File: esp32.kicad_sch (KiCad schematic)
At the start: 22 parts, among them J3 serial, Q2 Q_NPN_BCE, Q3 Q_NPN_BCE, U26 ESP32-WROOM-32D, U28 LMZM23601

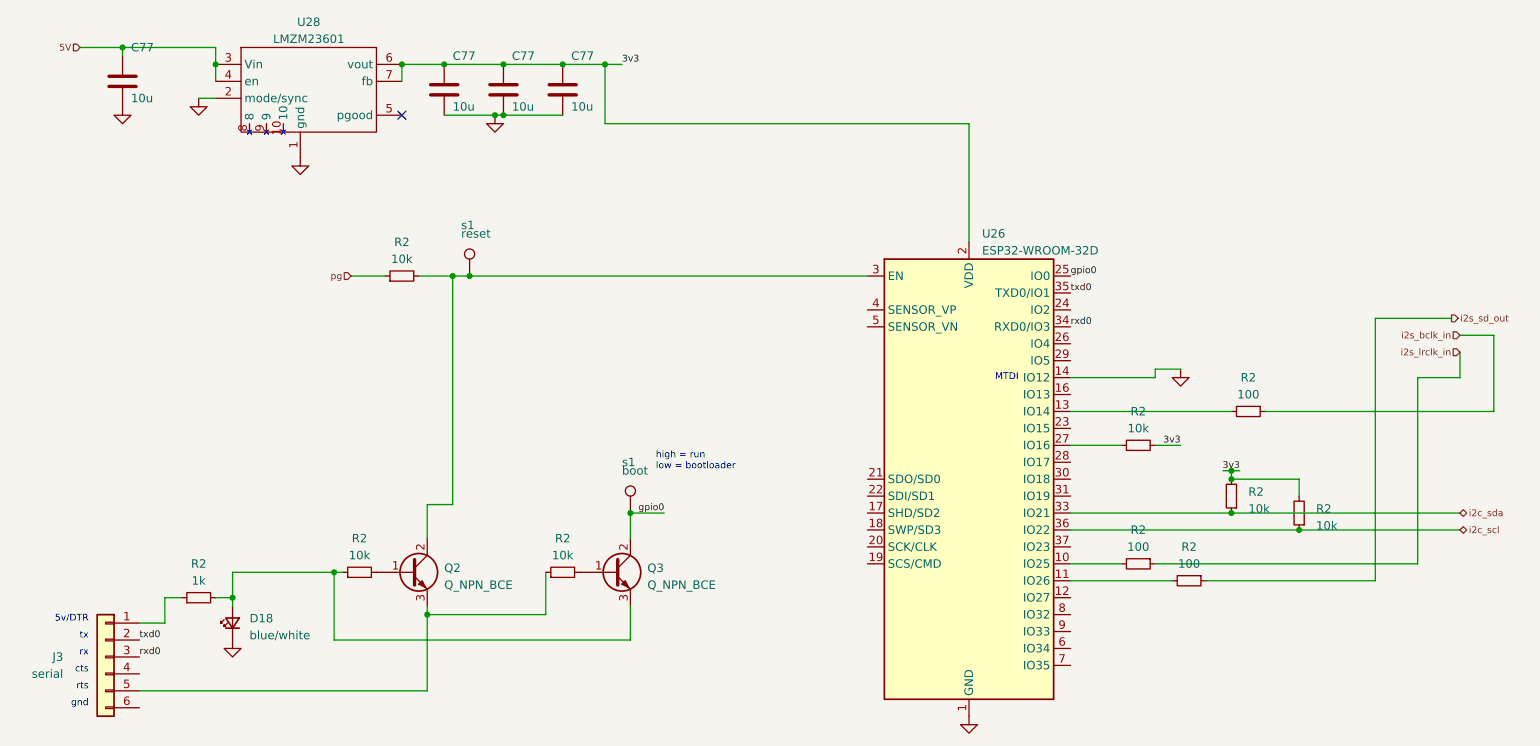
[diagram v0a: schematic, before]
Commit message: update to kicad 8
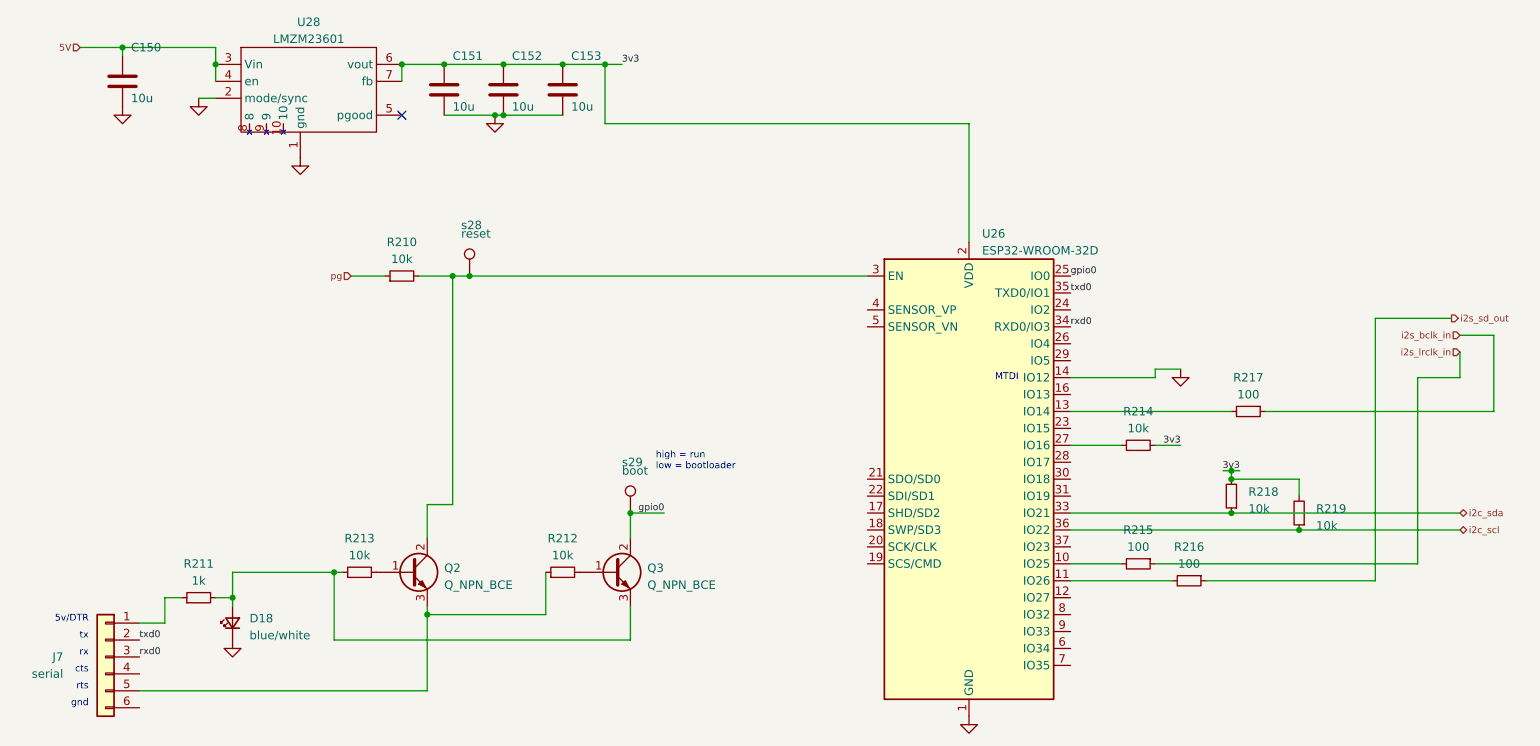
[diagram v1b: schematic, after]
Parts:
- renumbered C77 to C150, C77 to C151, C77 to C152, C77 to C153, J3 to J7, R2 to R210, R2 to R211, R2 to R212, R2 to R213, R2 to R214, R2 to R215, R2 to R216, R2 to R217, R2 to R218, R2 to R219, s1 to s28, s1 to s29

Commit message: schematic: some fixes
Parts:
- added R222: 10k, invendelirium_audio:R_0603, symbol Device:R_Small
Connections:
- net GND: now also R222.2; no longer U26.14 (IO12)
- new net: R222.1, U26.14 (IO12)
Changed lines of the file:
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@@
 	(wire
 		(pts
-			(xy 189.23 73.66) (xy 193.04 73.66)
+			(xy 191.77 73.66) (xy 195.58 73.66)
 		)
 		(stroke
@@
 	(wire
 		(pts
-			(xy 189.23 74.93) (xy 189.23 73.66)
+			(xy 191.77 74.93) (xy 191.77 73.66)
 		)
 		(stroke
@@
 	(wire
 		(pts
+			(xy 187.96 74.93) (xy 191.77 74.93)
+		)
+		(stroke
+			(width 0)
+			(type default)
+		)
+	)
+	(wire
+		(pts
 			(xy 222.25 105.41) (xy 196.85 105.41)
 		)
@@
 	(wire
 		(pts
-			(xy 176.53 74.93) (xy 189.23 74.93)
+			(xy 176.53 74.93) (xy 182.88 74.93)
 		)
 		(stroke
@@
 	(symbol
 		(lib_id "power:GND")
-		(at 193.04 73.66 0)
+		(at 195.58 73.66 0)
 		(unit 1)
 		(exclude_from_sim no)
@@
 		(fields_autoplaced yes)
 		(property "Reference" "#PWR0184"
-			(at 193.04 80.01 0)
+			(at 195.58 80.01 0)
 			(effects
 				(font
@@
 		)
 		(property "Value" "GND"
-			(at 193.04 78.74 0)
+			(at 195.58 78.74 0)
 			(effects
 				(font
@@
 		)
 		(property "Footprint" ""
-			(at 193.04 73.66 0)
+			(at 195.58 73.66 0)
 			(effects
 				(font
@@
 		)
 		(property "Datasheet" ""
-			(at 193.04 73.66 0)
+			(at 195.58 73.66 0)
 			(effects
 				(font
@@
 		)
 		(property "Description" ""
-			(at 193.04 73.66 0)
+			(at 195.58 73.66 0)
 			(effects
 				(font
@@
 					(unit 1)
 				)
+			)
+		)
+	)
+	(symbol
+		(lib_id "Device:R_Small")
+		(at 185.42 74.93 90)
+		(unit 1)
+		(exclude_from_sim no)
+		(in_bom yes)
+		(on_board yes)
+		(dnp no)
+		(fields_autoplaced yes)
+		(property "Reference" "R222"
+			(at 185.42 69.85 90)
+			(effects
+				(font
+					(size 1.27 1.27)
+				)
+			)
+		)
+		(property "Value" "10k"
+			(at 185.42 72.39 90)
+			(effects
+				(font
+					(size 1.27 1.27)
+				)
+			)
+		)
+		(property "Footprint" "invendelirium_audio:R_0603"
+			(at 185.42 74.93 0)
+			(effects
+				(font
+					(size 1.27 1.27)
+				)
+				(hide yes)
+			)
+		)
+		(property "Datasheet" "~"
+			(at 185.42 74.93 0)
+			(effects
+				(font
+					(size 1.27 1.27)
+				)
+				(hide yes)
+			)
+		)
+		(property "Description" ""
+			(at 185.42 74.93 0)
+			(effects
+				(font
+					(size 1.27 1.27)
+				)
+				(hide yes)
+			)
+		)
+		(pin "1"
+		)
+		(pin "2"
+		)
+		(instances
+			(project "uberamp1"
+				(path "/310059c1-d84b-43e2-9c9a-0e426c534a12/c7f5e7f4-a933-42eb-8650-67011ef6e24d"
+					(reference "R222")
+					(unit 1)
+				)

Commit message: updates
* add line out
* fix almost all erc
* some more random edits
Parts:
- U26: PN (none) -> ESP32-WROOM-32E-N16
- U28: PN (none) -> LMZM23601
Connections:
- net GND: now also J7.6 (Pin_6)
- no-connect marks 1 -> 24
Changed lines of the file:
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@@
+	)
+	(no_connect
+		(at 176.53 118.11)
+	)
+	(no_connect
+		(at 146.05 95.25)
+	)
+	(no_connect
+		(at 176.53 90.17)
+	)
+	(no_connect
+		(at 176.53 113.03)
+	)
+	(no_connect
+		(at 146.05 97.79)
+	)
+	(no_connect
+		(at 176.53 87.63)
+	)
+	(no_connect
+		(at 146.05 67.31)
+	)
+	(no_connect
+		(at 146.05 92.71)
+	)
+	(no_connect
+		(at 146.05 64.77)
+	)
+	(no_connect
+		(at 36.83 119.38)
+	)
+	(no_connect
+		(at 176.53 110.49)
+	)
+	(no_connect
+		(at 176.53 115.57)
+	)
+	(no_connect
+		(at 176.53 92.71)
+	)
+	(no_connect
+		(at 176.53 107.95)
 	)
 	(no_connect
 		(at 76.2 35.56)
+	)
+	(no_connect
+		(at 146.05 90.17)
+	)
+	(no_connect
+		(at 146.05 100.33)
+	)
+	(no_connect
+		(at 176.53 77.47)
+	)
+	(no_connect
+		(at 176.53 64.77)
+	)
+	(no_connect
+		(at 146.05 102.87)
+	)
+	(no_connect
+		(at 176.53 72.39)
+	)
+	(no_connect
+		(at 176.53 100.33)
+	)
+	(no_connect
+		(at 176.53 69.85)
+	)
+	(no_connect
+		(at 176.53 82.55)
 	)
 	(wire
@@
 	)
 	(symbol
+		(lib_id "power:GND")
+		(at 36.83 124.46 0)
+		(unit 1)
+		(exclude_from_sim no)
+		(in_bom yes)
+		(on_board yes)
+		(dnp no)
+		(fields_autoplaced yes)
+		(property "Reference" "#PWR0195"
+			(at 36.83 130.81 0)
+			(effects
+				(font
+					(size 1.27 1.27)
+				)
+				(hide yes)
+			)
+		)
+		(property "Value" "GND"
+			(at 36.83 129.54 0)
+			(effects
+				(font
+					(size 1.27 1.27)
+				)
+				(hide yes)
+			)
+		)
+		(property "Footprint" ""
+			(at 36.83 124.46 0)
+			(effects
+				(font
+					(size 1.27 1.27)
+				)
+				(hide yes)
+			)
+		)
+		(property "Datasheet" ""
+			(at 36.83 124.46 0)
+			(effects
+				(font
+					(size 1.27 1.27)
+				)
+				(hide yes)
+			)
+		)
+		(property "Description" ""
+			(at 36.83 124.46 0)
+			(effects
+				(font
+					(size 1.27 1.27)
+				)
+				(hide yes)
+			)
+		)
+		(pin "1"
+		)
+		(instances
+			(project "uberamp1"
+				(path "/310059c1-d84b-43e2-9c9a-0e426c534a12/c7f5e7f4-a933-42eb-8650-67011ef6e24d"
+					(reference "#PWR0195")
+					(unit 1)
+				)
+			)
+		)
+	)
+	(symbol
 		(lib_id "invendelirium_ic:LMZM23601")
 		(at 63.5 33.02 0)
@@
 		)
 		(property "Description" ""
+			(at 63.5 33.02 0)
+			(effects
+				(font
+					(size 1.27 1.27)
+				)
+				(hide yes)
+			)
+		)
+		(property "PN" "LMZM23601"
 			(at 63.5 33.02 0)
 			(effects
@@
 			(at 161.29 90.17 0)
 			(effects
+				(font
+					(size 1.27 1.27)
+				)
+				(hide yes)
+			)
+		)
+		(property "PN" "ESP32-WROOM-32E-N16"
+			(at 161.29 90.17 0)
+			(effects

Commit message: add power input +...
+ tons of fixes, footprint assignments, etc
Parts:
- renumbered C151 to CU28_1, C152 to CU28_2, C153 to CU28_3

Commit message: routing...
+ swap around dac channels, otherwise routing was crazy
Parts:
- U26: footprint RF_Module:ESP32-WROOM-32D -> invendelirium_audio:ESP32-WROOM-32D
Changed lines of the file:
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@@
 			)
 		)
-		(property "Footprint" "RF_Module:ESP32-WROOM-32D"
+		(property "Footprint" "invendelirium_audio:ESP32-WROOM-32D"
 			(at 177.8 124.46 0)
 			(effects

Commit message: lots of drc-related work
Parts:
- Q2, Q3: footprint PCM_4ms_Package_SOT:SOT23-3_PO123 -> invendelirium_general:SOT23-3_PO123
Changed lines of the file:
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@@
 			)
 		)
-		(property "Footprint" "PCM_4ms_Package_SOT:SOT23-3_PO123"
+		(property "Footprint" "invendelirium_general:SOT23-3_PO123"
 			(at 82.55 101.6 0)
 			(effects
@@
 			)
 		)
-		(property "Footprint" "PCM_4ms_Package_SOT:SOT23-3_PO123"
+		(property "Footprint" "invendelirium_general:SOT23-3_PO123"
 			(at 113.03 101.6 0)
 			(effects

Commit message: update some footprints
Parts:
- D18: footprint LED_SMD:LED_0805_2012Metric -> invendelirium_general:D_0805
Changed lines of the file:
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@@
 			)
 		)
-		(property "Footprint" "LED_SMD:LED_0805_2012Metric"
+		(property "Footprint" "invendelirium_general:D_0805"
 			(at 50.8 111.76 90)
 			(effects

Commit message: fill in some part numbers
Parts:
- s28, s29: now left out of the parts list
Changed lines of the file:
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@@
 		(unit 1)
 		(exclude_from_sim no)
-		(in_bom yes)
+		(in_bom no)
 		(on_board yes)
 		(dnp no)
@@
 		(unit 1)
 		(exclude_from_sim no)
-		(in_bom yes)
+		(in_bom no)
 		(on_board yes)
 		(dnp no)
